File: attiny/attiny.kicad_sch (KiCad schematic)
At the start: 11 parts, among them J1 arduino, J2 esp32, J3 cavalier, J4 Conn_01x01, U1 ATtiny85V-10S

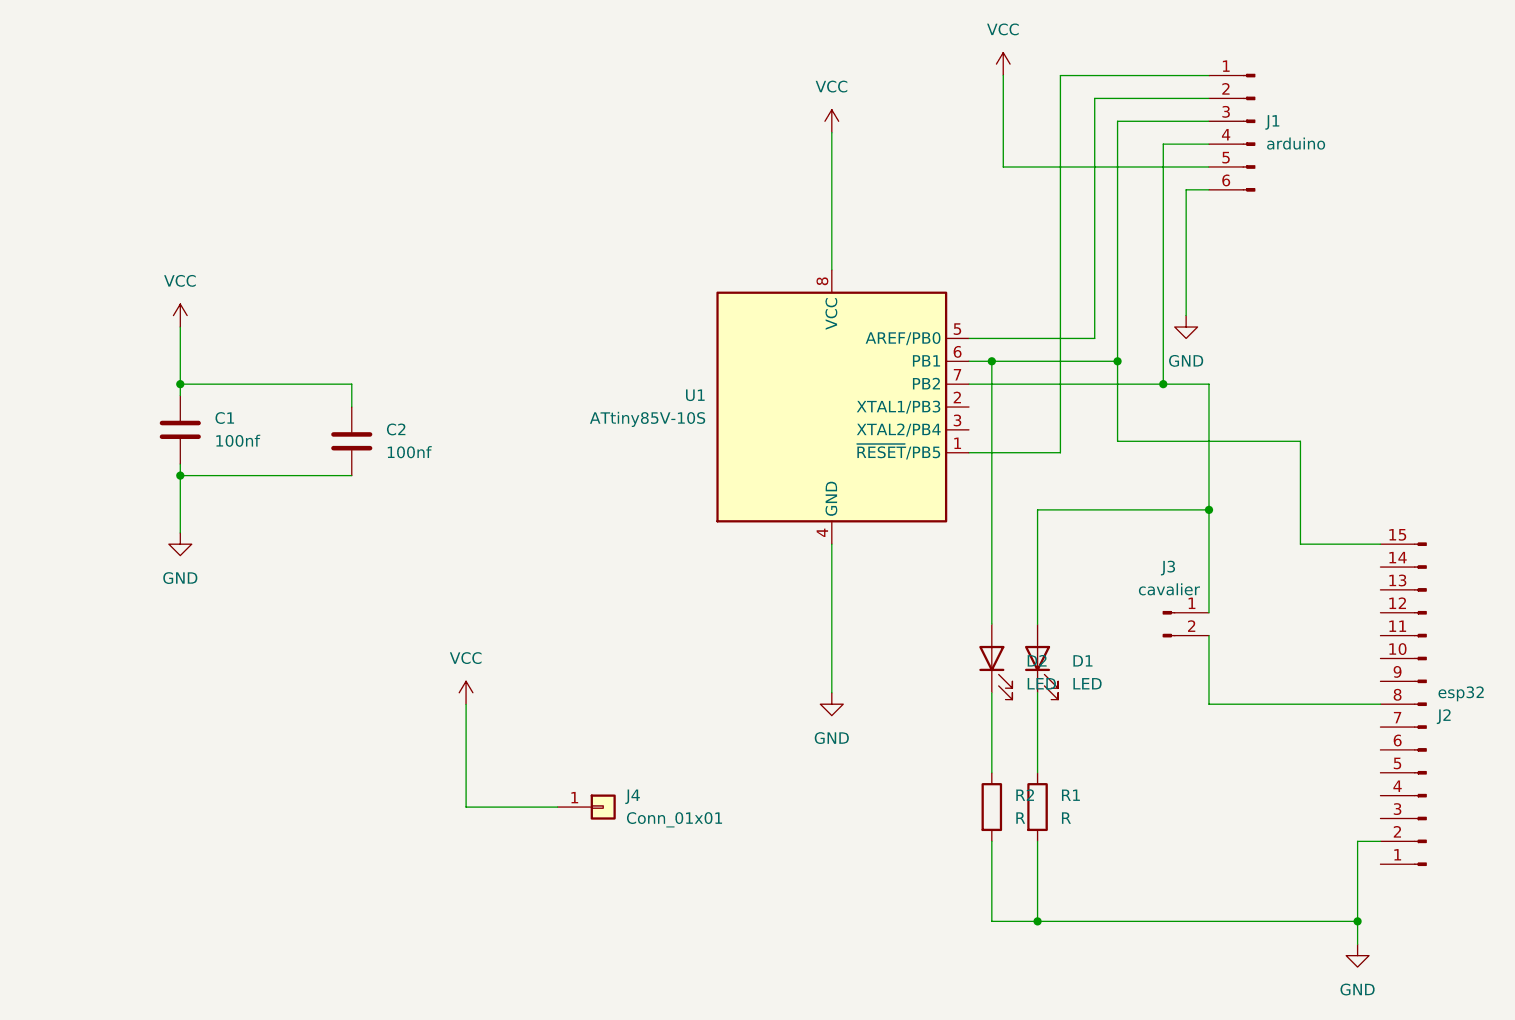
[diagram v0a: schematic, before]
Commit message: composant basic pour jlpcb (très petit dificilement soudable a la main)
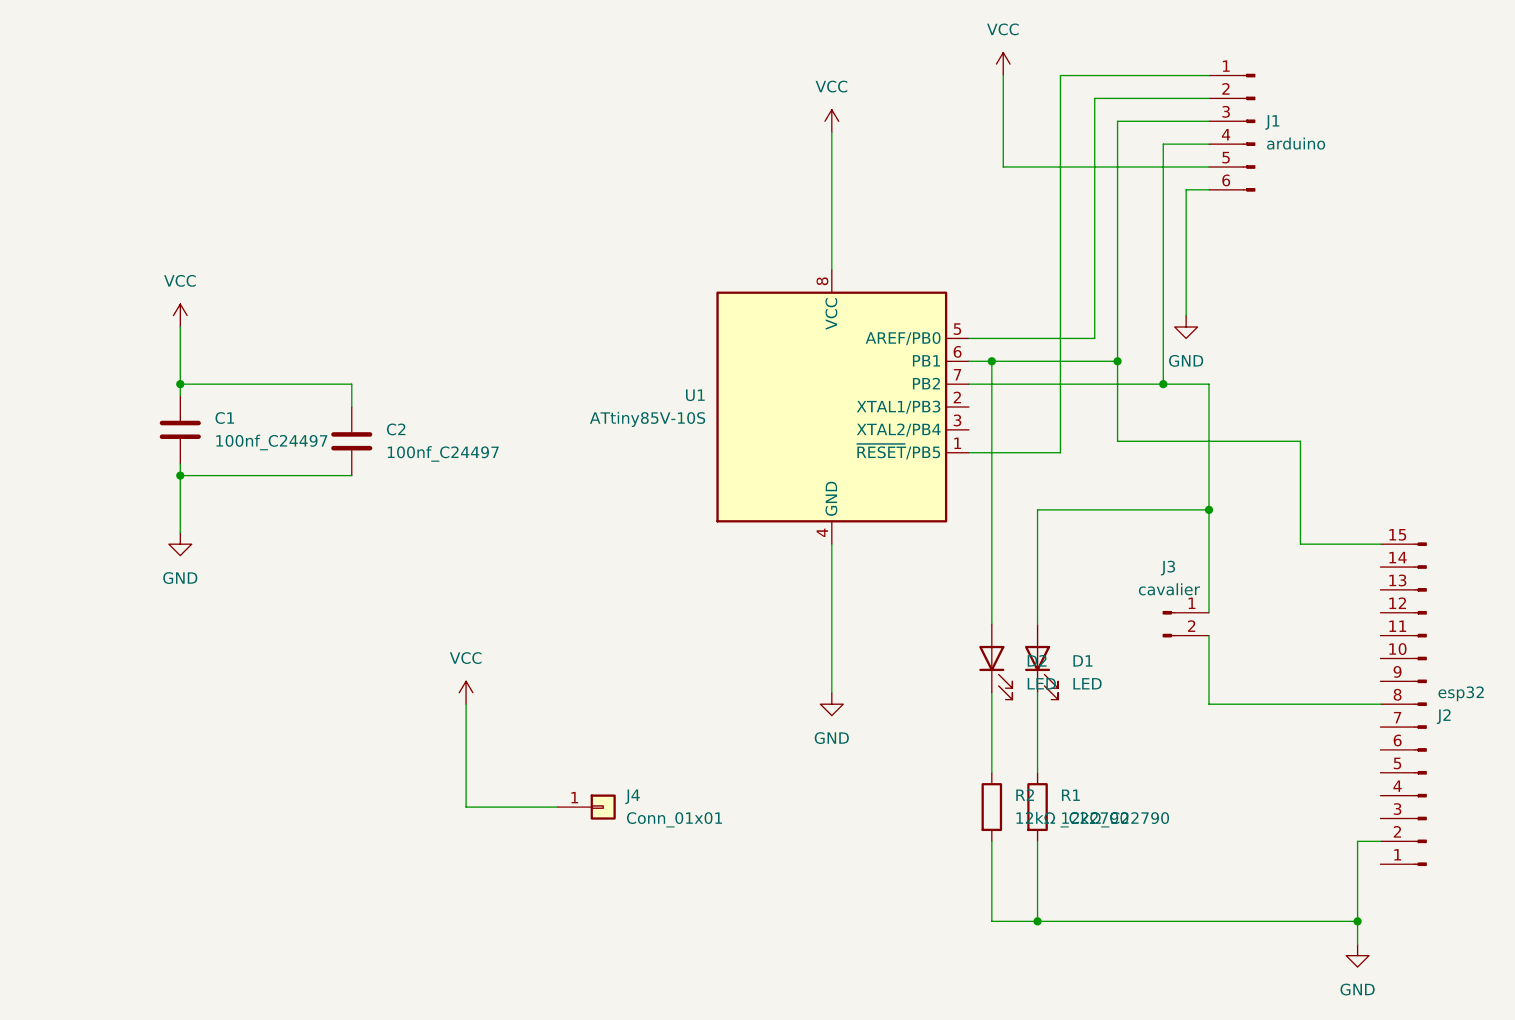
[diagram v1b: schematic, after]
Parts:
- C1, C2: value 100nf -> 100nf_C24497; footprint Capacitor_SMD:C_1206_3216Metric -> Capacitor_SMD:C_0201_0603Metric
- R1: value R -> 12kΩ_C22790; footprint LED_SMD:LED_1206_3216Metric_Pad1.42x1.75mm_HandSolder -> Resistor_SMD:R_0201_0603Metric
- R2: value R -> 12kΩ _C22790; footprint LED_SMD:LED_1206_3216Metric_Pad1.42x1.75mm_HandSolder -> Resistor_SMD:R_0201_0603Metric
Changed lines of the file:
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@@
 			)
 		)
-		(property "Value" "R"
+		(property "Value" "12kΩ_C22790"
 			(at 156.21 139.6999 0)
 			(effects
@@
 			)
 		)
-		(property "Footprint" "LED_SMD:LED_1206_3216Metric_Pad1.42x1.75mm_HandSolder"
+		(property "Footprint" "Resistor_SMD:R_0201_0603Metric"
 			(at 151.892 138.43 90)
 			(effects
@@
 			)
 		)
-		(property "Value" "100nf"
+		(property "Value" "100nf_C24497"
 			(at 62.23 97.7899 0)
 			(effects
@@
 			)
 		)
-		(property "Footprint" "Capacitor_SMD:C_1206_3216Metric"
+		(property "Footprint" "Capacitor_SMD:C_0201_0603Metric"
 			(at 59.3852 100.33 0)
 			(effects
@@
 			)
 		)
-		(property "Value" "R"
+		(property "Value" "12kΩ _C22790"
 			(at 151.13 139.6999 0)
 			(effects
@@
 			)
 		)
-		(property "Footprint" "LED_SMD:LED_1206_3216Metric_Pad1.42x1.75mm_HandSolder"
+		(property "Footprint" "Resistor_SMD:R_0201_0603Metric"
 			(at 146.812 138.43 90)
 			(effects
@@
 			)
 		)
-		(property "Value" "100nf"
+		(property "Value" "100nf_C24497"
 			(at 81.28 99.0599 0)
 			(effects
@@
 			)
 		)
-		(property "Footprint" "Capacitor_SMD:C_1206_3216Metric"
+		(property "Footprint" "Capacitor_SMD:C_0201_0603Metric"
 			(at 78.4352 101.6 0)
 			(effects

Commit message: acomposant pour production automatique chez jlcpcb environ 18€ 2 pcb assemblé et 3 non assemblé
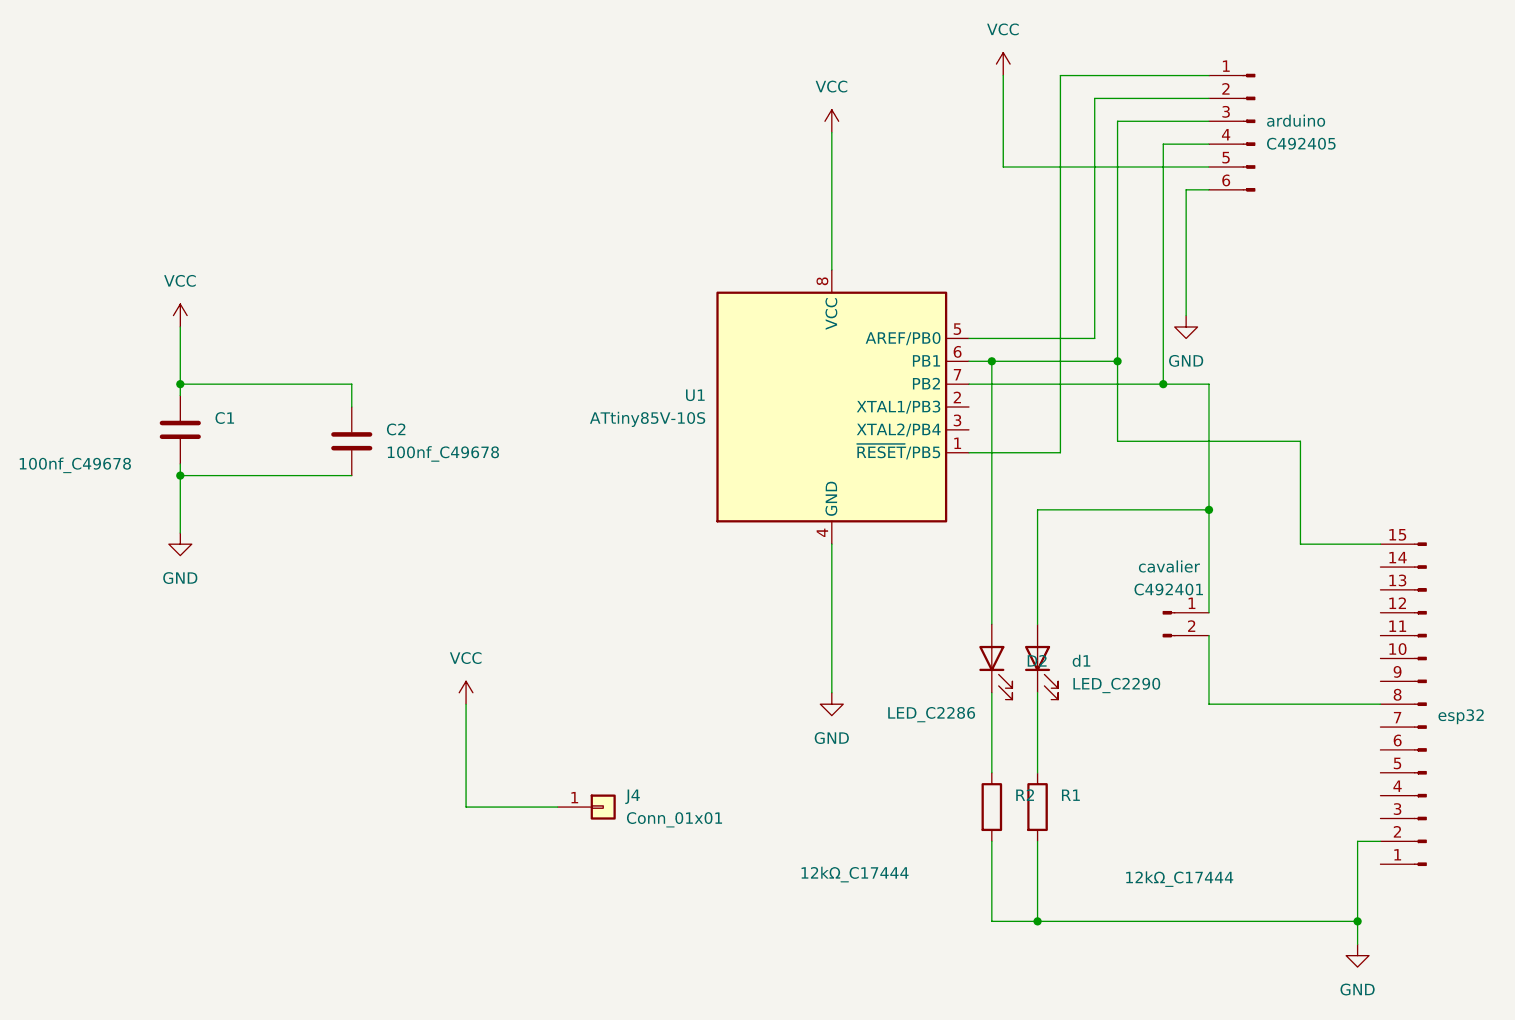
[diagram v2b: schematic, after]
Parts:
- C1, C2: value 100nf_C24497 -> 100nf_C49678; footprint Capacitor_SMD:C_0201_0603Metric -> Capacitor_SMD:C_0805_2012Metric
- D2: value LED -> LED_C2286; footprint LED_THT:LED_D1.8mm_W3.3mm_H2.4mm -> LED_SMD:LED_0603_1608Metric
- R1: value 12kΩ_C22790 -> 12kΩ_C17444; footprint Resistor_SMD:R_0201_0603Metric -> Resistor_SMD:R_0805_2012Metric
- R2: value 12kΩ _C22790 -> 12kΩ_C17444; footprint Resistor_SMD:R_0201_0603Metric -> Resistor_SMD:R_0805_2012Metric
- arduino: renamed from J1; value arduino -> C492405
- cavalier: renamed from J3; value cavalier -> C492401
- d1: renamed from D1; value LED -> LED_C2290; footprint LED_THT:LED_D1.8mm_W3.3mm_H2.4mm -> LED_SMD:LED_0603_1608Metric
- esp32: renamed from J2; value esp32 -> ~
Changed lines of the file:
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@@
 		(on_board yes)
 		(dnp no)
-		(fields_autoplaced yes)
 		(property "Reference" "D2"
 			(at 152.4 122.2374 90)
@@
 			)
 		)
-		(property "Value" "LED"
-			(at 152.4 124.7774 90)
+		(property "Value" "LED_C2286"
+			(at 136.906 128.016 90)
 			(effects
 				(font
@@
 			)
 		)
-		(property "Footprint" "LED_THT:LED_D1.8mm_W3.3mm_H2.4mm"
+		(property "Footprint" "LED_SMD:LED_0603_1608Metric"
 			(at 148.59 121.92 0)
 			(effects
@@
 		(on_board yes)
 		(dnp no)
-		(fields_autoplaced yes)
 		(property "Reference" "R1"
 			(at 156.21 137.1599 0)
@@
 			)
 		)
-		(property "Value" "12kΩ_C22790"
-			(at 156.21 139.6999 0)
+		(property "Value" "12kΩ_C17444"
+			(at 163.322 146.304 0)
 			(effects
 				(font
@@
 			)
 		)
-		(property "Footprint" "Resistor_SMD:R_0201_0603Metric"
+		(property "Footprint" "Resistor_SMD:R_0805_2012Metric"
 			(at 151.892 138.43 90)
 			(effects
@@
 		(on_board yes)
 		(dnp no)
-		(fields_autoplaced yes)
 		(property "Reference" "C1"
 			(at 62.23 95.2499 0)
@@
 			)
 		)
-		(property "Value" "100nf_C24497"
-			(at 62.23 97.7899 0)
+		(property "Value" "100nf_C49678"
+			(at 40.386 100.33 0)
 			(effects
 				(font
@@
 			)
 		)
-		(property "Footprint" "Capacitor_SMD:C_0201_0603Metric"
+		(property "Footprint" "Capacitor_SMD:C_0805_2012Metric"
 			(at 59.3852 100.33 0)
 			(effects
@@
 		(on_board yes)
 		(dnp no)
-		(fields_autoplaced yes)
 		(property "Reference" "R2"
 			(at 151.13 137.1599 0)
@@
 			)
 		)
-		(property "Value" "12kΩ _C22790"
-			(at 151.13 139.6999 0)
+		(property "Value" "12kΩ_C17444"
+			(at 127.254 145.796 0)
 			(effects
 				(font
@@
 			)
 		)
-		(property "Footprint" "Resistor_SMD:R_0201_0603Metric"
+		(property "Footprint" "Resistor_SMD:R_0805_2012Metric"
 			(at 146.812 138.43 90)
 			(effects
@@
 		(on_board yes)
 		(dnp no)
-		(property "Reference" "J2"
+		(property "Reference" "esp32"
 			(at 198.12 128.2701 0)
 			(effects
@@
 			)
 		)
-		(property "Value" "esp32"
+		(property "Value" "~"
 			(at 198.12 125.7301 0)
 			(effects
@@
 			(project ""
 				(path "/1890a4ac-20bc-4fd0-9813-4fbaeabd9094"
-					(reference "J2")
+					(reference "esp32")
 					(unit 1)
 				)
@@
 		(dnp no)
 		(fields_autoplaced yes)
-		(property "Reference" "J3"
+		(property "Reference" "cavalier"
 			(at 168.275 111.76 0)
 			(effects
@@
 			)
 		)
-		(property "Value" "cavalier"
+		(property "Value" "C492401"
 			(at 168.275 114.3 0)
 			(effects
@@
 			(project ""
 				(path "/1890a4ac-20bc-4fd0-9813-4fbaeabd9094"
-					(reference "J3")
+					(reference "cavalier")
 					(unit 1)
 				)
@@
 		(dnp no)
 		(fields_autoplaced yes)
-		(property "Reference" "J1"
+		(property "Reference" "arduino"
 			(at 179.07 62.2299 0)
 			(effects
@@
 			)
 		)
-		(property "Value" "arduino"
+		(property "Value" "C492405"
 			(at 179.07 64.7699 0)
 			(effects
@@
 			(project ""
 				(path "/1890a4ac-20bc-4fd0-9813-4fbaeabd9094"
-					(reference "J1")
+					(reference "arduino")
 					(unit 1)
 				)
@@
 			)
 		)
-		(property "Value" "100nf_C24497"
+		(property "Value" "100nf_C49678"
 			(at 81.28 99.0599 0)
 			(effects
@@
 			)
 		)
-		(property "Footprint" "Capacitor_SMD:C_0201_0603Metric"
+		(property "Footprint" "Capacitor_SMD:C_0805_2012Metric"
 			(at 78.4352 101.6 0)
 			(effects
@@
 		(dnp no)
 		(fields_autoplaced yes)
-		(property "Reference" "D1"
+		(property "Reference" "d1"
 			(at 157.48 122.2374 90)
 			(effects
@@
 			)
 		)
-		(property "Value" "LED"
+		(property "Value" "LED_C2290"
 			(at 157.48 124.7774 90)
 			(effects
@@
 			)
 		)
-		(property "Footprint" "LED_THT:LED_D1.8mm_W3.3mm_H2.4mm"
+		(property "Footprint" "LED_SMD:LED_0603_1608Metric"
 			(at 153.67 121.92 0)
 			(effects
@@
 			(project ""
 				(path "/1890a4ac-20bc-4fd0-9813-4fbaeabd9094"
-					(reference "D1")
-					(unit 1)
-				)
+					(reference "d1")
+					(unit 1)
+				)
